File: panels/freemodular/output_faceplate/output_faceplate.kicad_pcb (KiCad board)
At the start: 2 copper layers, 40.3 x 128.5 mm, 0 parts

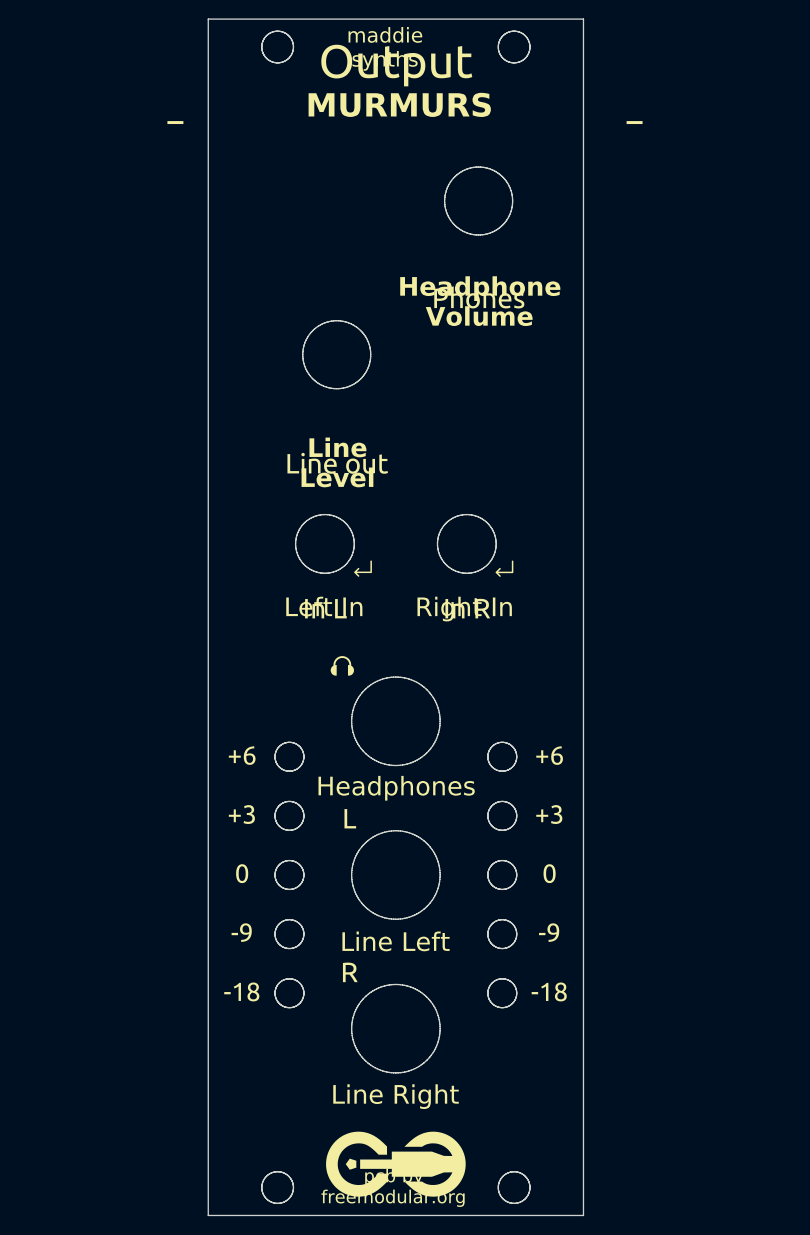
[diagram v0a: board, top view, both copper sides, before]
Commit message: mod2 firmwares, new faceplates
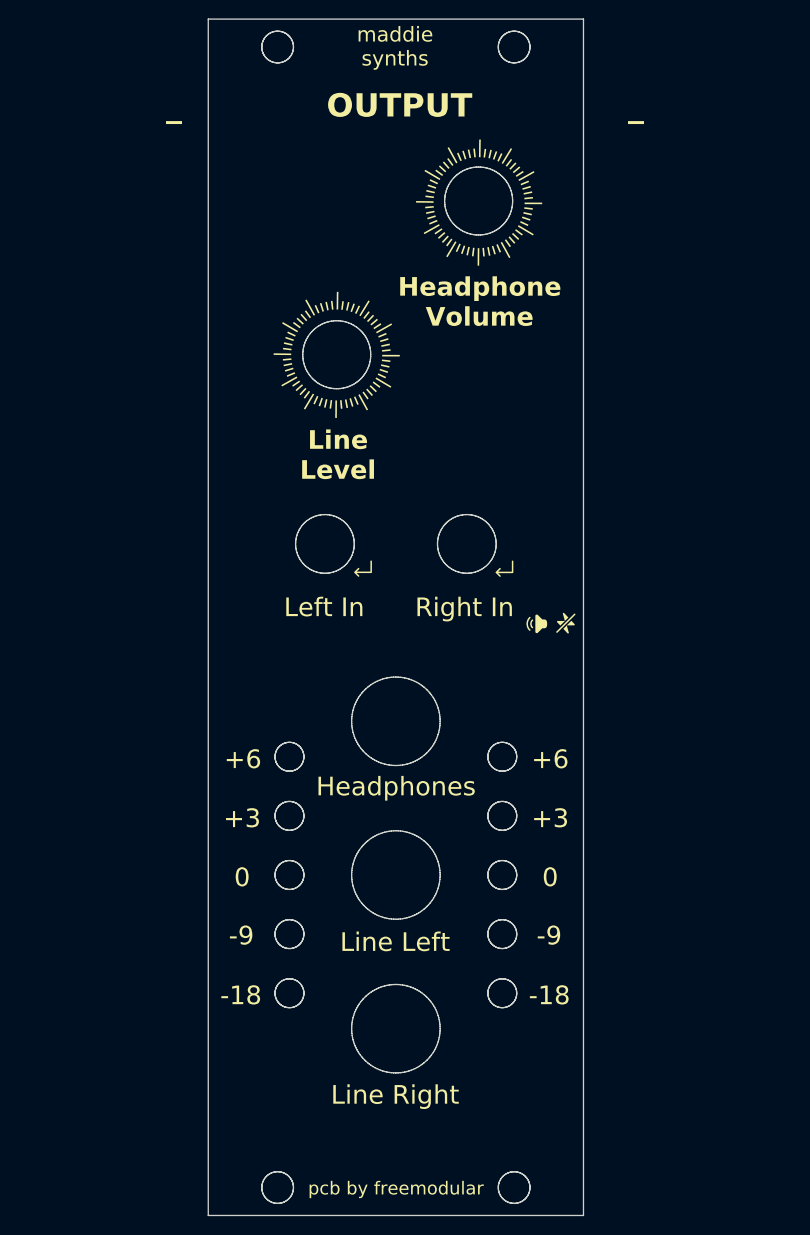
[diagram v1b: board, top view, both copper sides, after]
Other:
- board text added: "+3"
- board text added: "+6"
- board text added: "-18"
- board text added: "-9"
- board text added: "0"
- board text added: "_ OUTPUT _"
- board text added: "pcb by freemodular"
- board text removed: "_ MURMURS _"
- board text removed: "pcb by freemodular.org"
